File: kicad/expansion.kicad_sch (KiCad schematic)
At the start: 4 parts, among them J6 Conn_02x18_Top_Bottom, U35 74HC244, U36 74HC244, U37 74HC245

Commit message: Add caps and make initial placement
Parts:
- added C45, C46, C47: 100n, Capacitor_THT:C_Disc_D5.0mm_W2.5mm_P2.50mm, symbol Device:C
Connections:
- net GND: now also C45.2, C46.2, C47.2
- net VCC: now also C45.1, C46.1, C47.1

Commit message: Bugfixes, start routing
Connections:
- net at J6.31 (Pin_31), U36.7 (2Y2): no longer U37.1 (A->B)
- net at J6.32 (Pin_32), U36.5 (2Y1): now also U37.1 (A->B)
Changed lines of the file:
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@@
 	(paper "A4")
-	(junction
-		(at 166.37 134.62)
-		(diameter 0)
-		(color 0 0 0 0)
-	)
 	(junction
 		(at 161.29 101.6)
@@
 	)
 	(junction
+		(at 165.1 132.08)
+		(diameter 0)
+		(color 0 0 0 0)
+	)
+	(junction
 		(at 161.29 109.22)
 		(diameter 0)
@@
 		)
 	)
-	(wire
-		(pts
-			(xy 166.37 134.62) (xy 214.63 134.62)
-		)
-		(stroke
-			(width 0)
-			(type default)
-		)
-	)
 	(bus
 		(pts
@@
 	(wire
 		(pts
+			(xy 165.1 132.08) (xy 214.63 132.08)
+		)
+		(stroke
+			(width 0)
+			(type default)
+		)
+	)
+	(wire
+		(pts
 			(xy 152.4 81.28) (xy 182.88 81.28)
 		)
@@
 	(wire
 		(pts
-			(xy 214.63 134.62) (xy 214.63 93.98)
-		)
-		(stroke
+			(xy 214.63 93.98) (xy 214.63 132.08)
+		)
+		(stroke

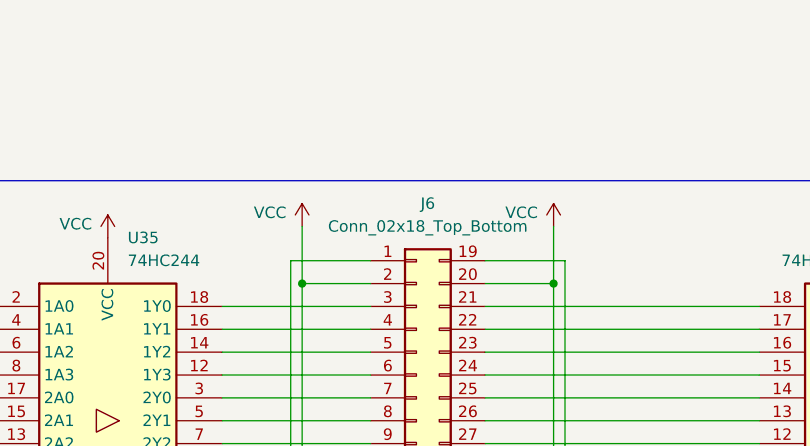
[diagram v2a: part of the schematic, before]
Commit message: hw: Finished rev B
Changelog:
- added fuse for the expansion port,
- added silkscreen symbols.
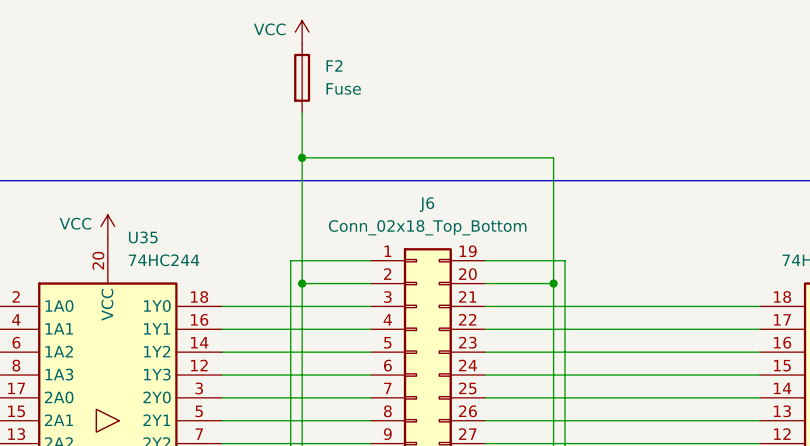
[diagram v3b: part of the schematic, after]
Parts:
- added F2: Fuse, PCM_Fuse_AKL:Fuse_Littelfuse_395Series, symbol Device:Fuse
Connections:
- net VCC: now also F2.1; no longer J6.17 (Pin_17), J6.2 (Pin_2), J6.20 (Pin_20), J6.35 (Pin_35)
- new net: F2.2, J6.17 (Pin_17), J6.2 (Pin_2), J6.20 (Pin_20), J6.35 (Pin_35)
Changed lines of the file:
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@@
 	)
 	(junction
+		(at 132.08 54.61)
+		(diameter 0)
+		(color 0 0 0 0)
+	)
+	(junction
 		(at 160.02 68.58)
 		(diameter 0)
@@
 	(wire
 		(pts
-			(xy 132.08 68.58) (xy 132.08 62.23)
+			(xy 132.08 54.61) (xy 132.08 68.58)
 		)
 		(stroke
@@
 	(wire
 		(pts
+			(xy 160.02 54.61) (xy 132.08 54.61)
+		)
+		(stroke
+			(width 0)
+			(type default)
+		)
+	)
+	(wire
+		(pts
 			(xy 167.64 93.98) (xy 167.64 113.03)
 		)
@@
 	(wire
 		(pts
-			(xy 160.02 68.58) (xy 160.02 62.23)
+			(xy 160.02 54.61) (xy 160.02 68.58)
 		)
 		(stroke
@@
 	(wire
 		(pts
+			(xy 132.08 54.61) (xy 132.08 49.53)
+		)
+		(stroke
+			(width 0)
+			(type default)
+		)
+	)
+	(wire
+		(pts
 			(xy 161.29 101.6) (xy 161.29 109.22)
 		)
@@
 	)
 	(symbol
+		(lib_id "power:VCC")
+		(at 132.08 41.91 0)
+		(unit 1)
+		(exclude_from_sim no)
+		(in_bom yes)
+		(on_board yes)
+		(dnp no)
+		(property "Reference" "#PWR0192"
+			(at 132.08 45.72 0)
+			(effects
+				(font
+					(size 1.27 1.27)
+				)
+				(hide yes)
+			)
+		)
+		(property "Value" "VCC"
+			(at 128.524 40.386 0)
+			(effects
+				(font
+					(size 1.27 1.27)
+				)
+			)
+		)
+		(property "Footprint" ""
+			(at 132.08 41.91 0)
+			(effects
+				(font
+					(size 1.27 1.27)
+				)
+				(hide yes)
+			)
+		)
+		(property "Datasheet" ""
+			(at 132.08 41.91 0)
+			(effects
+				(font
+					(size 1.27 1.27)
+				)
+				(hide yes)
+			)
+		)
+		(property "Description" "Power symbol creates a global label with name \"VCC\""
+			(at 132.08 41.91 0)
+			(effects
+				(font
+					(size 1.27 1.27)
+				)
+				(hide yes)
+			)
+		)
+		(pin "1"
+		)
+		(instances
+			(project "fella"
+				(path "/0e49b66d-39aa-4a48-b9a1-8037366b6d94/51f1375c-7d5b-4ef6-9c62-05d307c98d71"
+					(reference "#PWR0192")
+					(unit 1)
+				)
+			)
+		)
+	)
+	(symbol
 		(lib_id "power:GND")
 		(at 49.53 88.9 0)
@@
 	)
 	(symbol
-		(lib_id "power:VCC")
-		(at 132.08 62.23 0)
+		(lib_id "Device:C")
+		(at 49.53 85.09 0)
 		(unit 1)
 		(exclude_from_sim no)
@@
 		(on_board yes)
 		(dnp no)
-		(property "Reference" "#PWR091"
-			(at 132.08 66.04 0)
+		(fields_autoplaced yes)
+		(property "Reference" "C45"
+			(at 53.34 83.8199 0)
 			(effects
 				(font
 					(size 1.27 1.27)
 				)
-				(hide yes)
+				(justify left)
 			)
 		)
-		(property "Value" "VCC"
-			(at 128.524 60.706 0)
+		(property "Value" "100n"
+			(at 53.34 86.3599 0)
 			(effects
 				(font
 					(size 1.27 1.27)
 				)
+				(justify left)
 			)
 		)
-		(property "Footprint" ""
-			(at 132.08 62.23 0)
+		(property "Footprint" "Capacitor_THT:C_Disc_D5.0mm_W2.5mm_P2.50mm"
+			(at 50.4952 88.9 0)
 			(effects
 				(font
@@
 			)
 		)
-		(property "Datasheet" ""
-			(at 132.08 62.23 0)
+		(property "Datasheet" "~"
+			(at 49.53 85.09 0)
 			(effects
 				(font
@@
 			)
 		)
-		(property "Description" "Power symbol creates a global label with name \"VCC\""
-			(at 132.08 62.23 0)
+		(property "Description" "Unpolarized capacitor"
+			(at 49.53 85.09 0)
 			(effects
 				(font
@@
 			)
 		)
+		(pin "2"
+		)
 		(pin "1"
 		)
@@
 			(project "fella"
 				(path "/0e49b66d-39aa-4a48-b9a1-8037366b6d94/51f1375c-7d5b-4ef6-9c62-05d307c98d71"
-					(reference "#PWR091")
+					(reference "C45")
 					(unit 1)
 				)
@@
 	)
 	(symbol
-		(lib_id "Device:C")
-		(at 49.53 85.09 0)
+		(lib_id "Device:Fuse")
+		(at 132.08 45.72 0)
 		(unit 1)
 		(exclude_from_sim no)
@@
 		(dnp no)
 		(fields_autoplaced yes)
-		(property "Reference" "C45"
-			(at 53.34 83.8199 0)
+		(property "Reference" "F2"
+			(at 134.62 44.4499 0)
 			(effects
 				(font
@@
 			)
 		)
-		(property "Value" "100n"
-			(at 53.34 86.3599 0)
+		(property "Value" "Fuse"
+			(at 134.62 46.9899 0)
 			(effects
 				(font
@@
 			)
 		)
-		(property "Footprint" "Capacitor_THT:C_Disc_D5.0mm_W2.5mm_P2.50mm"
-			(at 50.4952 88.9 0)
+		(property "Footprint" "PCM_Fuse_AKL:Fuse_Littelfuse_395Series"
+			(at 130.302 45.72 90)
 			(effects
 				(font
@@
 		)
 		(property "Datasheet" "~"
-			(at 49.53 85.09 0)
+			(at 132.08 45.72 0)
 			(effects
 				(font
@@
 			)
 		)
-		(property "Description" "Unpolarized capacitor"
-			(at 49.53 85.09 0)
+		(property "Description" "Fuse"
+			(at 132.08 45.72 0)
 			(effects
 				(font
@@
 			)
 		)
-		(pin "2"
-		)
 		(pin "1"
 		)
+		(pin "2"
+		)
 		(instances
 			(project "fella"
 				(path "/0e49b66d-39aa-4a48-b9a1-8037366b6d94/51f1375c-7d5b-4ef6-9c62-05d307c98d71"
-					(reference "C45")
+					(reference "F2")
 					(unit 1)
 				)
@@
 					(unit 1)
 				)
-			)
-		)
-	)
-	(symbol
-		(lib_id "power:VCC")
-		(at 160.02 62.23 0)
-		(unit 1)
-		(exclude_from_sim no)
-		(in_bom yes)
-		(on_board yes)
-		(dnp no)
-		(property "Reference" "#PWR092"
-			(at 160.02 66.04 0)
-			(effects
-				(font
-					(size 1.27 1.27)
-				)
-				(hide yes)
-			)
-		)
-		(property "Value" "VCC"
-			(at 156.464 60.706 0)
-			(effects
-				(font
-					(size 1.27 1.27)
-				)
-			)
-		)
-		(property "Footprint" ""
-			(at 160.02 62.23 0)
-			(effects
-				(font
-					(size 1.27 1.27)
-				)
-				(hide yes)
-			)
-		)
-		(property "Datasheet" ""
-			(at 160.02 62.23 0)
-			(effects
-				(font
-					(size 1.27 1.27)
-				)
-				(hide yes)
-			)
-		)
-		(property "Description" "Power symbol creates a global label with name \"VCC\""
-			(at 160.02 62.23 0)
-			(effects
-				(font
-					(size 1.27 1.27)
-				)
-				(hide yes)
-			)
-		)
-		(pin "1"
-		)
-		(instances
-			(project "fella"
-				(path "/0e49b66d-39aa-4a48-b9a1-8037366b6d94/51f1375c-7d5b-4ef6-9c62-05d307c98d71"
-					(reference "#PWR092")
-					(unit 1)
-				)

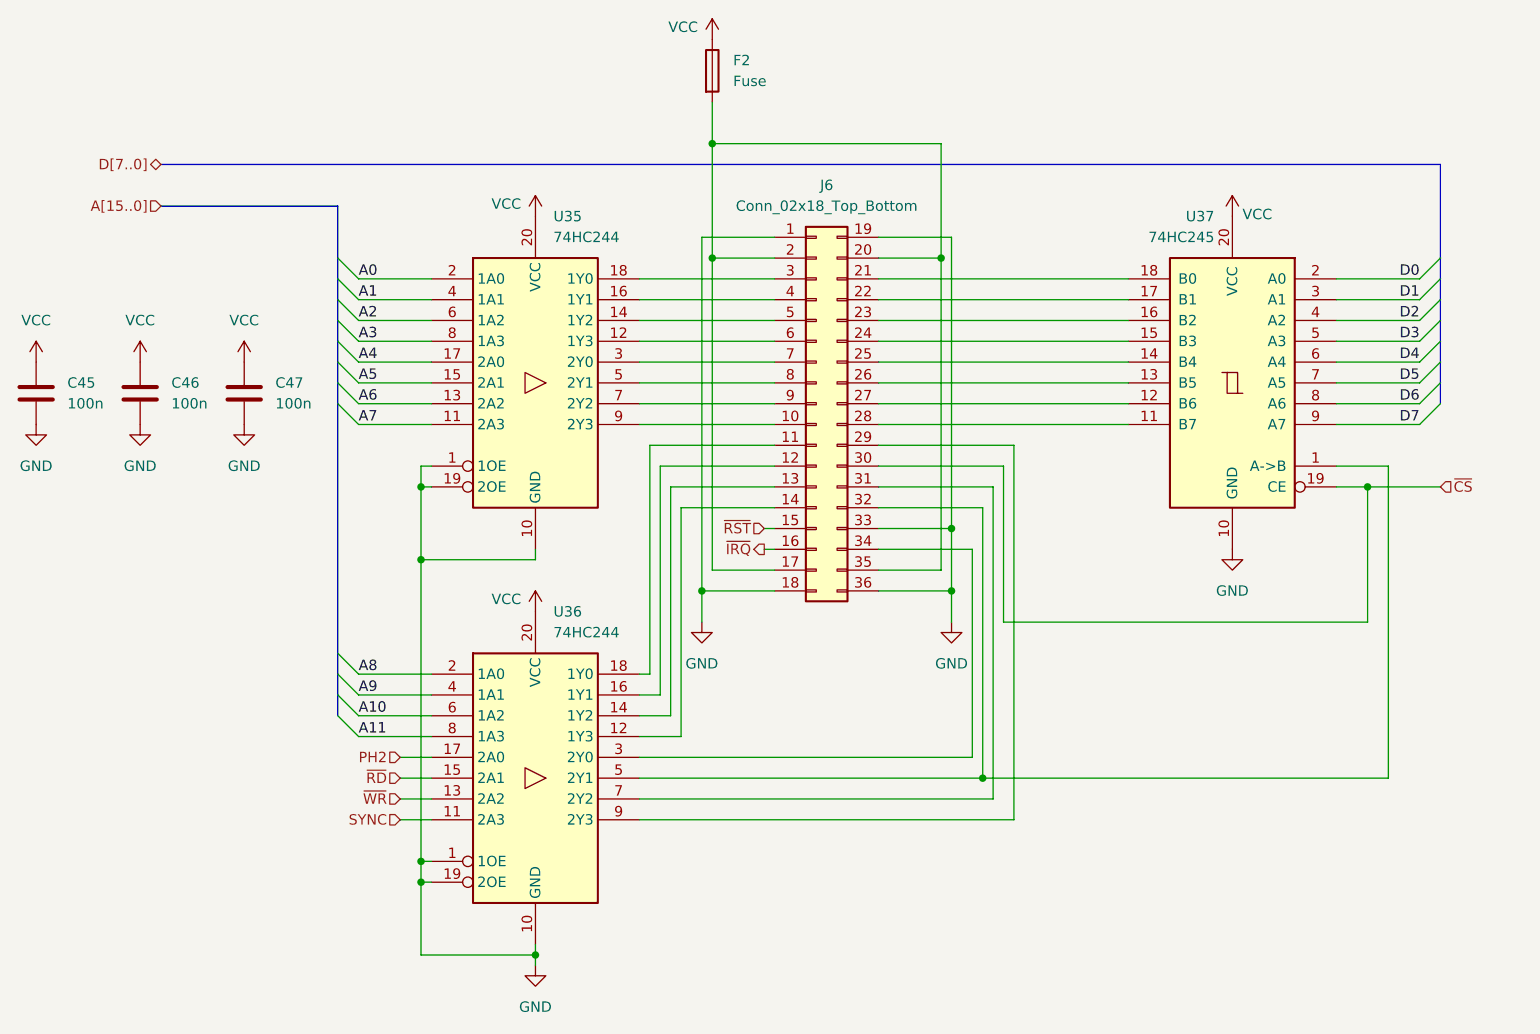
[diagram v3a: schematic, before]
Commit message: hw: revision C
Major changes:
- ROM space has been extended from 16 KiB to 32 KiB
- dynamic RAM option has been removed
- RAM size has been reduced from 32 KiB to 24 KiB
- expansion slot now replaces internal ROM, does not
  have dedicated memory space anymore
- place all I/O within a compactish 8 KiB
- move PH2 gating to /RD and /WR signals
- PCB redo (mechanicaly compatible)
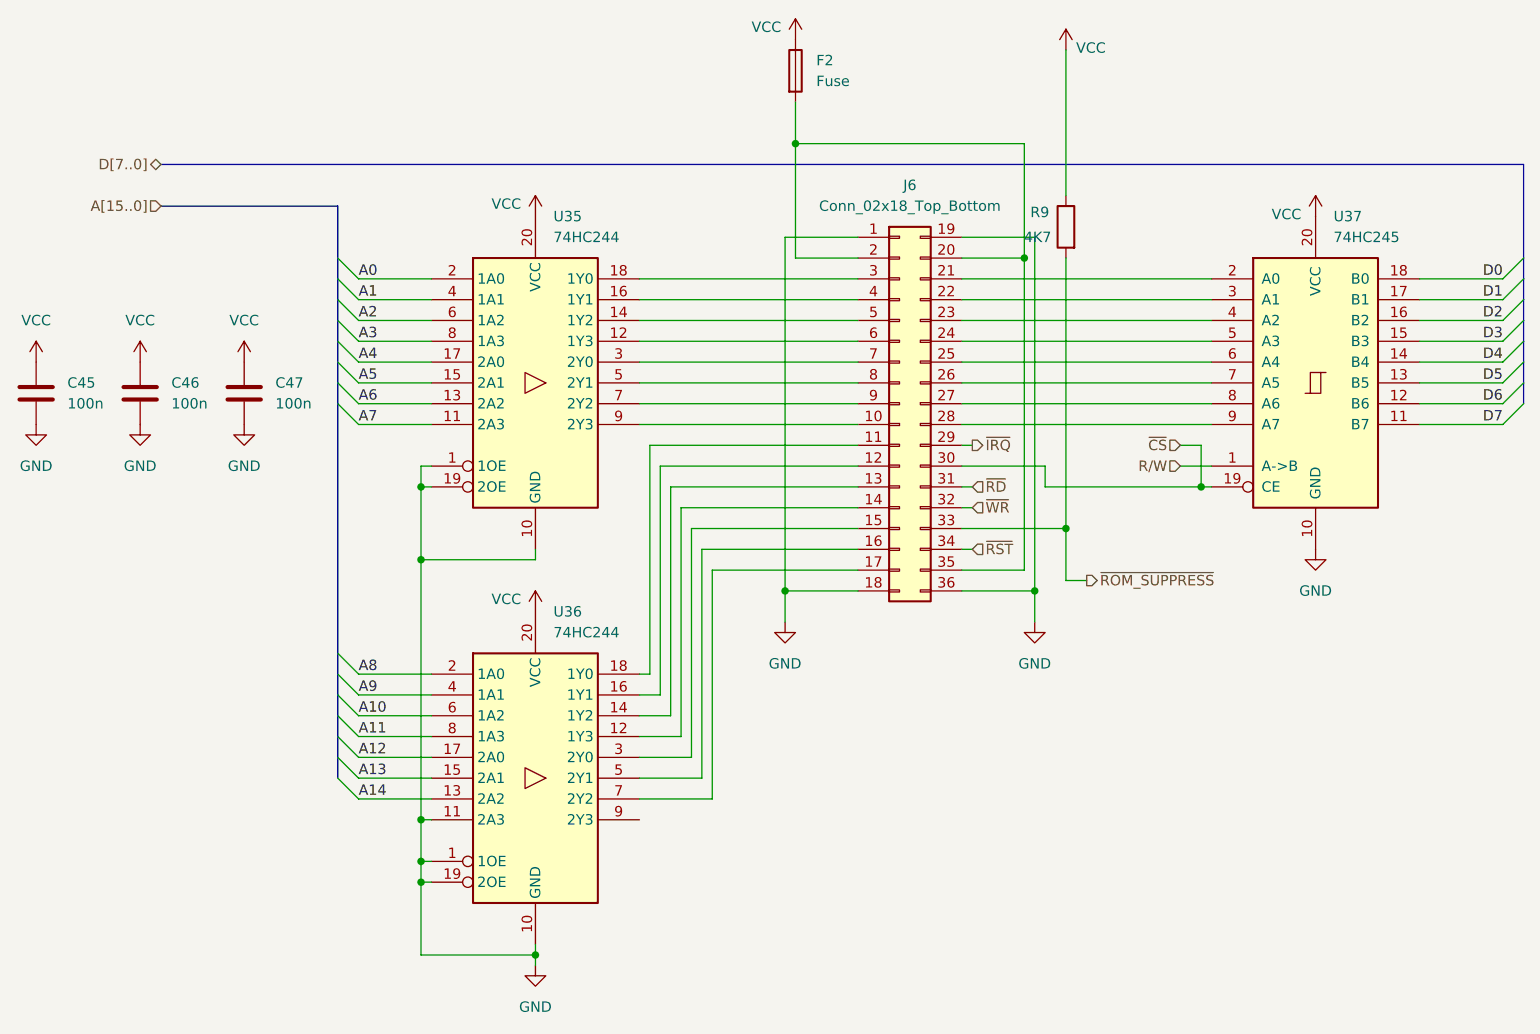
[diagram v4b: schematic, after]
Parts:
- added R9: 4K7, Resistor_THT:R_Axial_DIN0207_L6.3mm_D2.5mm_P7.62mm_Horizontal, symbol Device:R
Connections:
- net SYNC is gone; now on net GND: U36.11 (2A3)
- net D0: now also U37.18 (B0); no longer U37.2 (A0)
- net D1: now also U37.17 (B1); no longer U37.3 (A1)
- net D2: now also U37.16 (B2); no longer U37.4 (A2)
- net D3: now also U37.15 (B3); no longer U37.5 (A3)
- net D4: now also U37.14 (B4); no longer U37.6 (A4)
- net D5: now also U37.13 (B5); no longer U37.7 (A5)
- net D6: now also U37.12 (B6); no longer U37.8 (A6)
- net D7: now also U37.11 (B7); no longer U37.9 (A7)
- net GND: no longer J6.33 (Pin_33)
- net VCC: now also R9.1
- net ~{IRQ}: now also J6.29 (Pin_29); no longer J6.16 (Pin_16)
- net ~{RD}: now also J6.31 (Pin_31); no longer U36.15 (2A1)
- net ~{RST}: now also J6.34 (Pin_34); no longer J6.15 (Pin_15)
- net ~{WR}: now also J6.32 (Pin_32); no longer U36.13 (2A2)
- net at J6.28 (Pin_28): now also U37.9 (A7); no longer U37.11 (B7)
- net at J6.27 (Pin_27): now also U37.8 (A6); no longer U37.12 (B6)
- net at J6.26 (Pin_26): now also U37.7 (A5); no longer U37.13 (B5)
- net at J6.25 (Pin_25): now also U37.6 (A4); no longer U37.14 (B4)
- net at J6.24 (Pin_24): now also U37.5 (A3); no longer U37.15 (B3)
- net at J6.23 (Pin_23): now also U37.4 (A2); no longer U37.16 (B2)
- net at J6.22 (Pin_22): now also U37.3 (A1); no longer U37.17 (B1)
- net at J6.21 (Pin_21): now also U37.2 (A0); no longer U37.18 (B0)
- net at F2.2, J6.2 (Pin_2), J6.20 (Pin_20)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: no longer J6.17 (Pin_17)
- net at U36.9 (2Y3): no longer J6.29 (Pin_29)
- net at U36.7 (2Y2): now also J6.17 (Pin_17); no longer J6.31 (Pin_31)
- net at U36.3 (2Y0): now also J6.15 (Pin_15); no longer J6.34 (Pin_34)
- net PH2 renamed A12
- new net: J6.16 (Pin_16), U36.5 (2Y1)
- new net A13: U36.15 (2A1)
- new net A14: U36.13 (2A2)
- new net R/W: U37.1 (A->B)
- new net ~{ROM_SUPPRESS}: J6.33 (Pin_33), R9.2
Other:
- moved on the sheet: F2, J6, U37

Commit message: hw: rev D - replace DB25 connector footprint with available one
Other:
- company: (none) -> A.K.
- title: (none) -> Expansion slot
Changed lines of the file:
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@@
 (kicad_sch
-	(version 20231120)
+	(version 20250114)
 	(generator "eeschema")
-	(generator_version "8.0")
+	(generator_version "9.0")
 	(paper "A4")
+	(title_block
+		(title "Expansion slot")
+		(date "2025-08-04")
+		(rev "D")
+		(company "A.K.")
+	)
 	(junction
 		(at 96.52 105.41)
